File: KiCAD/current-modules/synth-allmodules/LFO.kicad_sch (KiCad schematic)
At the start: 56 parts, among them Q10 BC547, Q11 BC547, U12 TL074, U13 TL074, U14 TL072

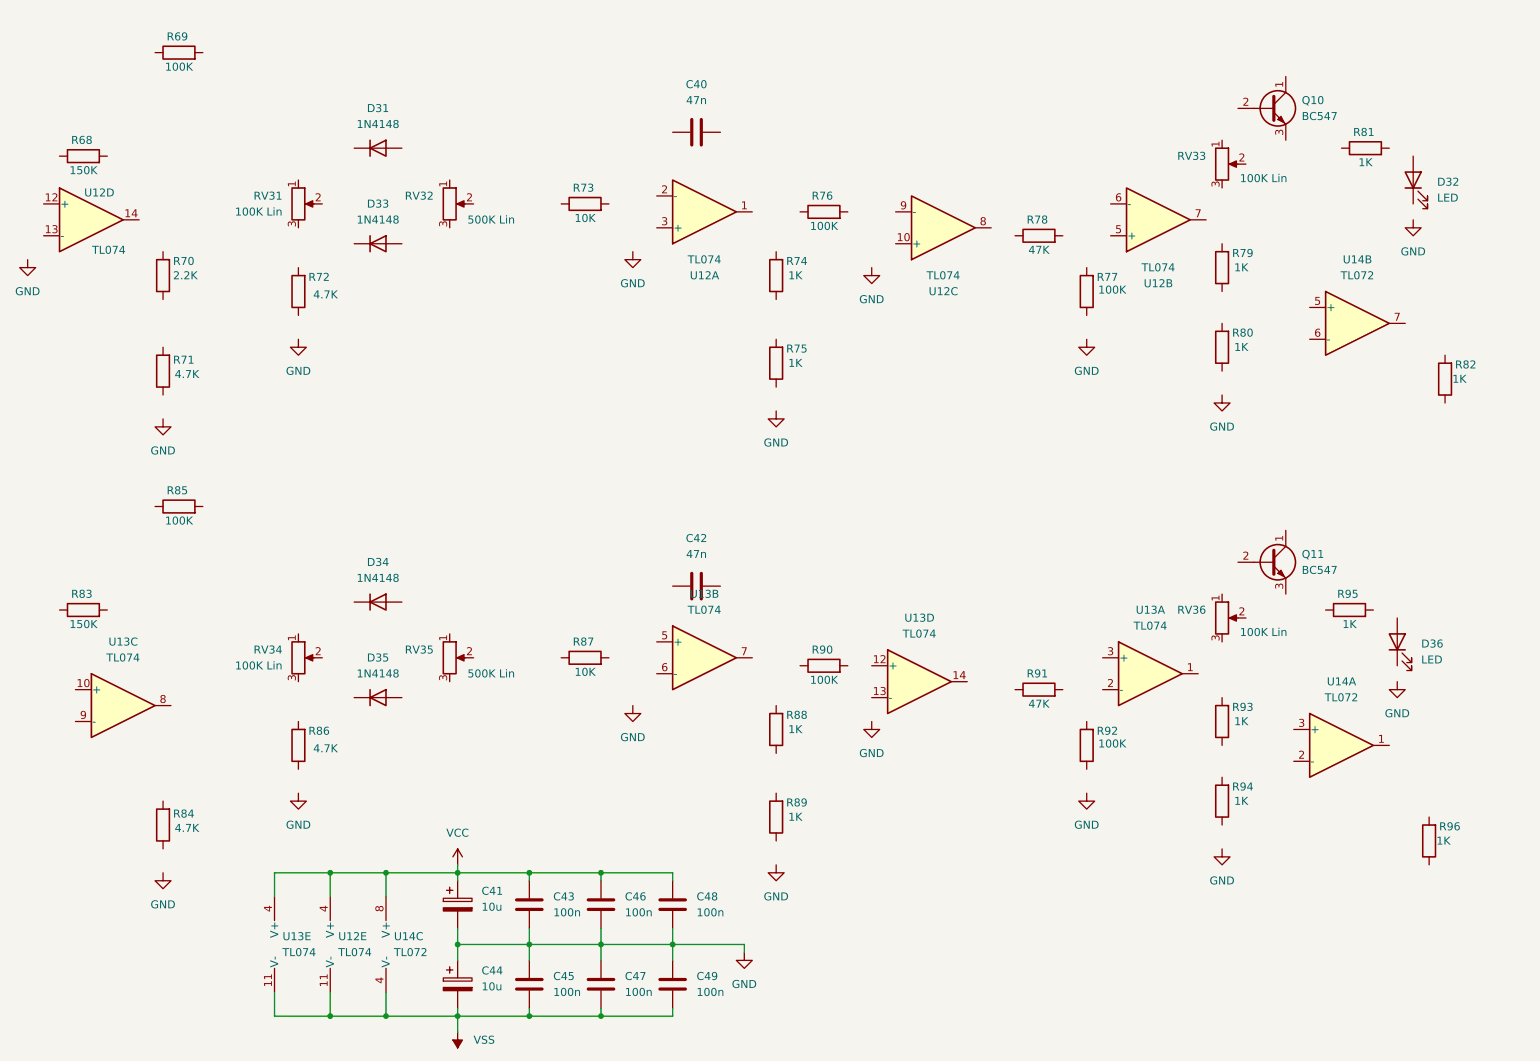
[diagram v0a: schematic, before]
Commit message: Wiring and Labelling Start
Additions:
- Output labels
- uC function labels
Changes:
- Wired first LFO module
Removals:
- None
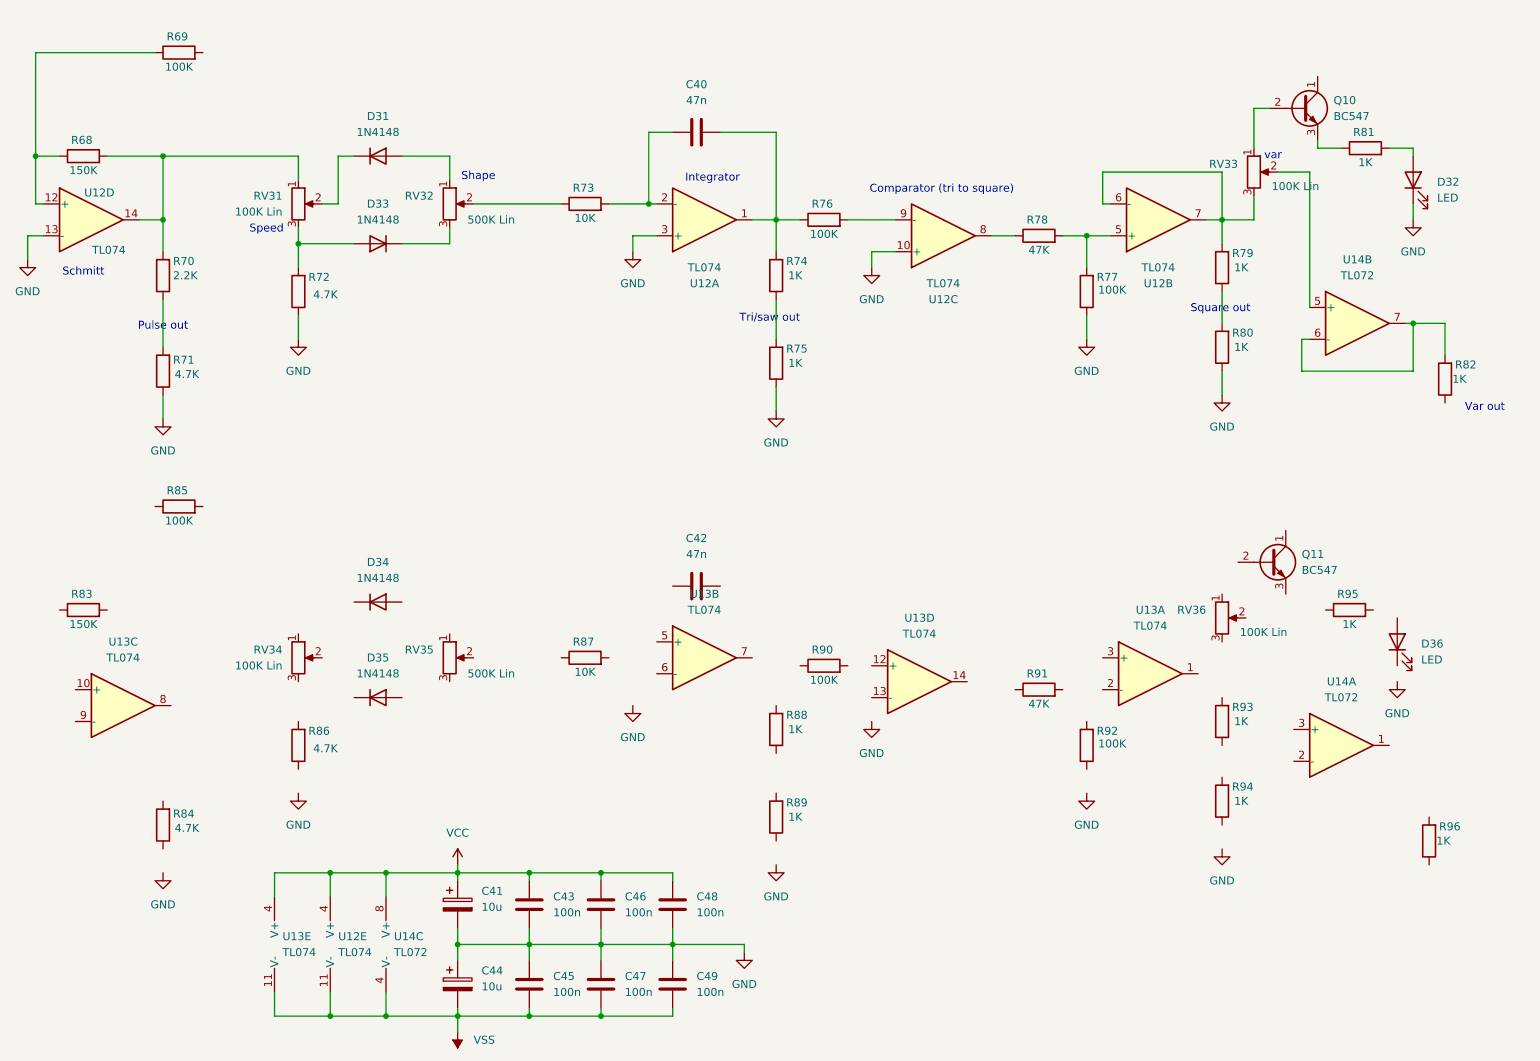
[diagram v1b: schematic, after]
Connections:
- net GND: now also D32.1 (K), R71.1, R72.1, R75.1, R77.1, R80.1, U12.10 (+), U12.13 (-), U12.3 (+)
- net at R78.1: now also U12.8
- net at R78.2: now also R77.2, U12.5 (+)
- net at R79.1: now also R80.2
- net at R79.2: now also RV33.3, U12.6 (-), U12.7
- net at D33.1 (K): now also RV32.3
- net at D33.2 (A): now also R72.2, RV31.3
- net at D31.1 (K): now also RV31.2
- net at D31.2 (A): now also RV32.1
- net at R70.1: now also R71.2
- net at R70.2: now also R68.2, RV31.1, U12.14
- net at R73.1: now also RV32.2
- net at R73.2: now also C40.1, U12.2 (-)
- net at U12.9 (-): now also R76.2
- net at RV33.1: now also Q10.2 (B)
- net at RV33.2: now also U14.5 (+)
- net at D32.2 (A): now also R81.2
- net at R68.1: now also R69.1, U12.12 (+)
- net at R76.1: now also C40.2, R74.2, U12.1
- net at U14.6 (-): now also R82.2, U14.7
- net at R74.1: now also R75.2
- net at R81.1: now also Q10.3 (E)
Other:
- note added: "Comparator (tri to square)"
- note added: "Integrator"
- note added: "Pulse out"
- note added: "Schmitt"
- note added: "Shape"
- note added: "Speed"
- note added: "Square out"
- note added: "Tri/saw out"
- note added: "Var out"
- note added: "var"
- moved on the sheet: D31, D33, Q10, R76, RV33, U12A, U12C

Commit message: Tweaks
Additions:
- Little bits remaining on first module
Changes:
- None
Removals:
- None
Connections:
- net VCC: now also Q10.1 (C)
- net at Q10.2 (B), RV33.1: now also C40.2, R69.2, R74.2, R76.1, U12.1
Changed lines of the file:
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@@
 	)
 	(junction
+		(at 151.13 35.56)
+		(diameter 0)
+		(color 0 0 0 0)
+	)
+	(junction
 		(at 53.34 49.53)
 		(diameter 0)
@@
 	)
 	(junction
+		(at 227.33 31.75)
+		(diameter 0)
+		(color 0 0 0 0)
+	)
+	(junction
 		(at 53.34 39.37)
 		(diameter 0)
@@
 	)
 	(junction
+		(at 151.13 22.86)
+		(diameter 0)
+		(color 0 0 0 0)
+	)
+	(junction
 		(at 200.66 52.07)
 		(diameter 0)
@@
 	(wire
 		(pts
+			(xy 227.33 22.86) (xy 227.33 31.75)
+		)
+		(stroke
+			(width 0)
+			(type default)
+		)
+	)
+	(wire
+		(pts
 			(xy 80.01 153.67) (xy 88.9 153.67)
 		)
@@
 	(wire
 		(pts
+			(xy 59.69 22.86) (xy 151.13 22.86)
+		)
+		(stroke
+			(width 0)
+			(type default)
+		)
+	)
+	(wire
+		(pts
+			(xy 151.13 22.86) (xy 151.13 35.56)
+		)
+		(stroke
+			(width 0)
+			(type default)
+		)
+	)
+	(wire
+		(pts
 			(xy 227.33 49.53) (xy 222.25 49.53)
 		)
@@
 	(wire
 		(pts
+			(xy 237.49 22.86) (xy 237.49 26.67)
+		)
+		(stroke
+			(width 0)
+			(type default)
+		)
+	)
+	(wire
+		(pts
 			(xy 151.13 76.2) (xy 151.13 80.01)
 		)
@@
 	(wire
 		(pts
+			(xy 151.13 22.86) (xy 227.33 22.86)
+		)
+		(stroke
+			(width 0)
+			(type default)
+		)
+	)
+	(wire
+		(pts
 			(xy 123.19 165.1) (xy 123.19 167.64)
 		)
@@
 					(unit 1)
 				)
+			)
+		)
+	)
+	(symbol
+		(lib_id "power:VCC")
+		(at 237.49 22.86 0)
+		(unit 1)
+		(body_style 1)
+		(exclude_from_sim no)
+		(in_bom yes)
+		(on_board yes)
+		(in_pos_files yes)
+		(dnp no)
+		(fields_autoplaced yes)
+		(property "Reference" "#PWR0105"
+			(at 237.49 26.67 0)
+			(hide yes)
+			(show_name no)
+			(do_not_autoplace no)
+			(effects
+				(font
+					(size 1.27 1.27)
+				)
+			)
+		)
+		(property "Value" "VCC"
+			(at 237.49 17.78 0)
+			(show_name no)
+			(do_not_autoplace no)
+			(effects
+				(font
+					(size 1.27 1.27)
+				)
+			)
+		)
+		(property "Footprint" ""
+			(at 237.49 22.86 0)
+			(hide yes)
+			(show_name no)
+			(do_not_autoplace no)
+			(effects
+				(font
+					(size 1.27 1.27)
+				)
+			)
+		)
+		(property "Datasheet" ""
+			(at 237.49 22.86 0)
+			(hide yes)
+			(show_name no)
+			(do_not_autoplace no)
+			(effects
+				(font
+					(size 1.27 1.27)
+				)
+			)
+		)
+		(property "Description" "Power symbol creates a global label with name \"VCC\""
+			(at 237.49 22.86 0)
+			(hide yes)
+			(show_name no)
+			(do_not_autoplace no)
+			(effects
+				(font
+					(size 1.27 1.27)
+				)
+			)
+		)
+		(pin "1"
+		)
+		(instances
+			(project "synth-allmodules"
+				(path "/f3152922-b7ee-45aa-a88a-669787bc63c5/57297c67-a21a-4420-a1b2-76a0b3559e30"
+					(reference "#PWR0105")
+					(unit 1)
+				)

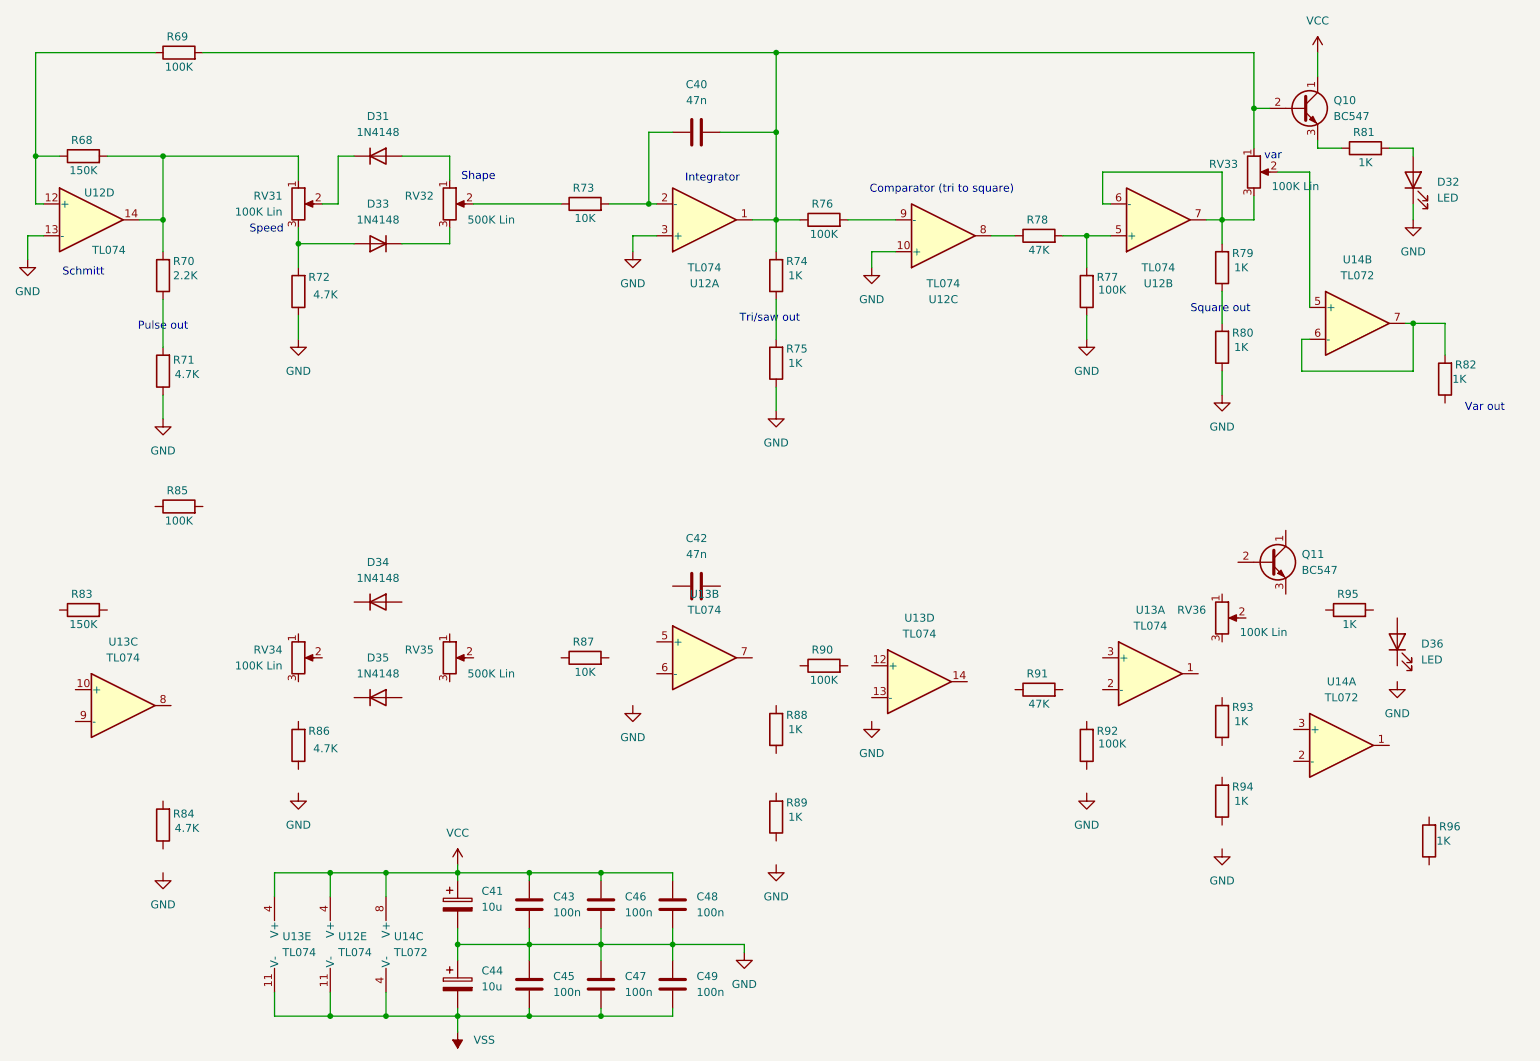
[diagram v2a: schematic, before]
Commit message: Second LFO module wired
Additions:
- Connected components for second LFO module
Changes:
- None
Removals:
- None
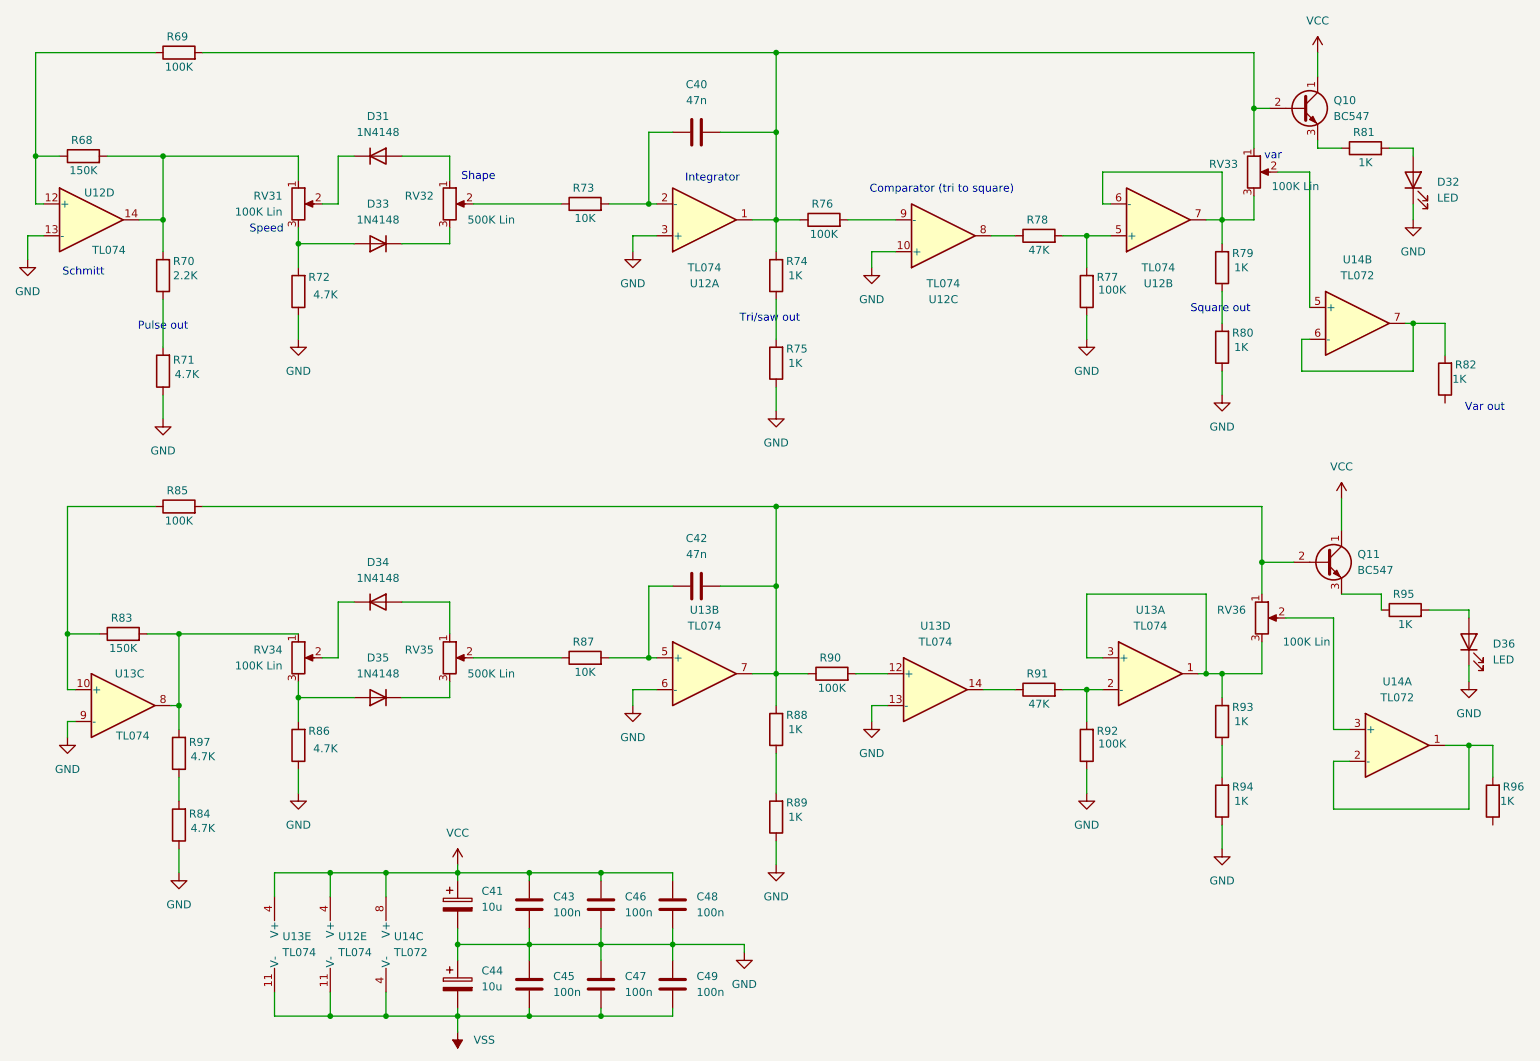
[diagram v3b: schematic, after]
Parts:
- added R97: 4.7K, symbol Device:R
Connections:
- net GND: now also D36.1 (K), R84.1, R86.1, R89.1, R92.1, R94.1, U13.13 (-), U13.6 (-), U13.9 (-)
- net VCC: now also Q11.1 (C)
- net at R95.1: now also Q11.3 (E)
- net at R95.2: now also D36.2 (A)
- net at R93.1: now also R94.2
- net at R93.2: now also RV36.3, U13.1, U13.3 (+)
- net at D34.1 (K): now also RV34.2
- net at D34.2 (A): now also RV35.1
- net at R89.2: now also R88.1
- net at R85.1: now also R83.1, U13.10 (+)
- net at R85.2: now also C42.2, Q11.2 (B), R88.2, R90.1, RV36.1, U13.7
- net at U13.12 (+): now also R90.2
- net at U13.14: now also R91.1
- net at R84.2: now also R97.1
- net at R86.2: now also D35.2 (A), RV34.3
- net at U14.1: now also R96.2, U14.2 (-)
- net at U14.3 (+): now also RV36.2
- net at R83.2: now also RV34.1, U13.8, R97.2
- net at C42.1: now also R87.2, U13.5 (+)
- net at U13.2 (-): now also R91.2, R92.2
- net at D35.1 (K): now also RV35.3
- net at RV35.2: now also R87.1
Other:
- moved on the sheet: D35, D36, Q11, R83, R84, R90, R95, R96, RV36, U13B, U13D, U14A
